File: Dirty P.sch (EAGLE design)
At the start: 23 parts, among them J1 NMJ6HCD2, J2 NMJ6HCD2, SW1 FOOT_SW, U1 MMBT3906, U2 MMBT3906, U3 MMBT3906

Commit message: switched to 4MM caps for 10uF
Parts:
- C1, C6: device MF_Passives:CAPACITOR_P_6.3MM -> MF_Passives:CAPACITOR_P_4MM
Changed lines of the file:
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@@
 <?xml version="1.0" encoding="utf-8"?>
 <!DOCTYPE eagle SYSTEM "eagle.dtd">
-<eagle version="6.6.0">
+<eagle version="6.5.0">
 <drawing>
 <settings>
@@
 <parts>
 <part name="J1" library="PP_Connectors" deviceset="TRS_SWITCHED" device="NMJ6HCD2" value="NMJ6HCD2"/>
-<part name="C1" library="MF_Passives" deviceset="CAPACITOR_P" device="_6.3MM" value="10uF"/>
+<part name="C1" library="MF_Passives" deviceset="CAPACITOR_P" device="_4MM" value="10uF"/>
 <part name="C2" library="MF_Passives" deviceset="CAPACITOR_NP" device="_0805" value="0.1uF"/>
 <part name="R1" library="MF_Passives" deviceset="RESISTOR" device="_0805" value="10K"/>
@@
 <part name="BATT1" library="PP_Connectors" deviceset="BATTERY" device="12BH611-GR" value="12BH611-GR"/>
 <part name="LEVEL" library="PP_Electromechanical" deviceset="POTENTIOMETER" device="PTD901" value="PTD901-2015K-A104"/>
-<part name="C6" library="MF_Passives" deviceset="CAPACITOR_P" device="_6.3MM" value="10uF"/>
+<part name="C6" library="MF_Passives" deviceset="CAPACITOR_P" device="_4MM" value="10uF"/>
 <part name="SW1" library="PP_Electromechanical" deviceset="SPDT" device="FOOT_SW" value="FOOT_SW"/>
 <part name="ATTACK" library="PP_Electromechanical" deviceset="POTENTIOMETER" device="PTD901" value="PTD901-2015K-B102"/>

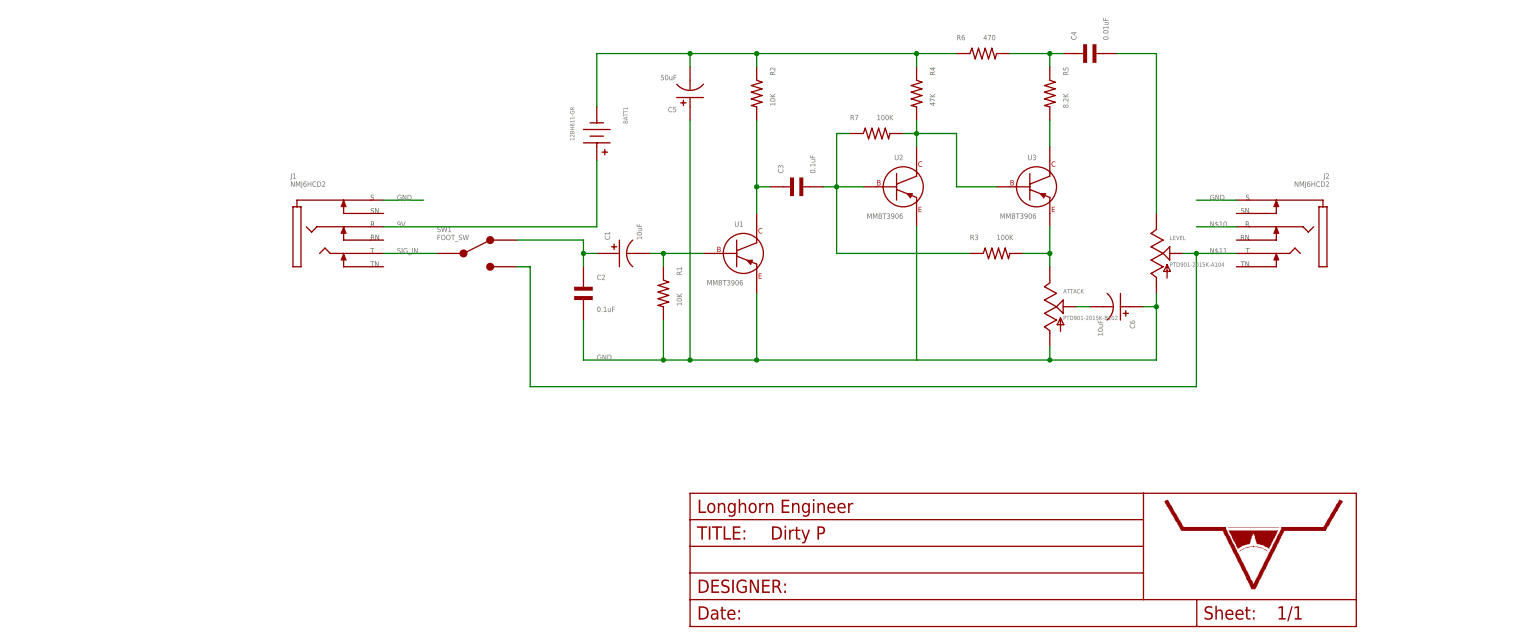
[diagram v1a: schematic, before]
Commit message: REV2: Bass switch. Bias Pot added. Fixed connectors. Added space for Bosses.
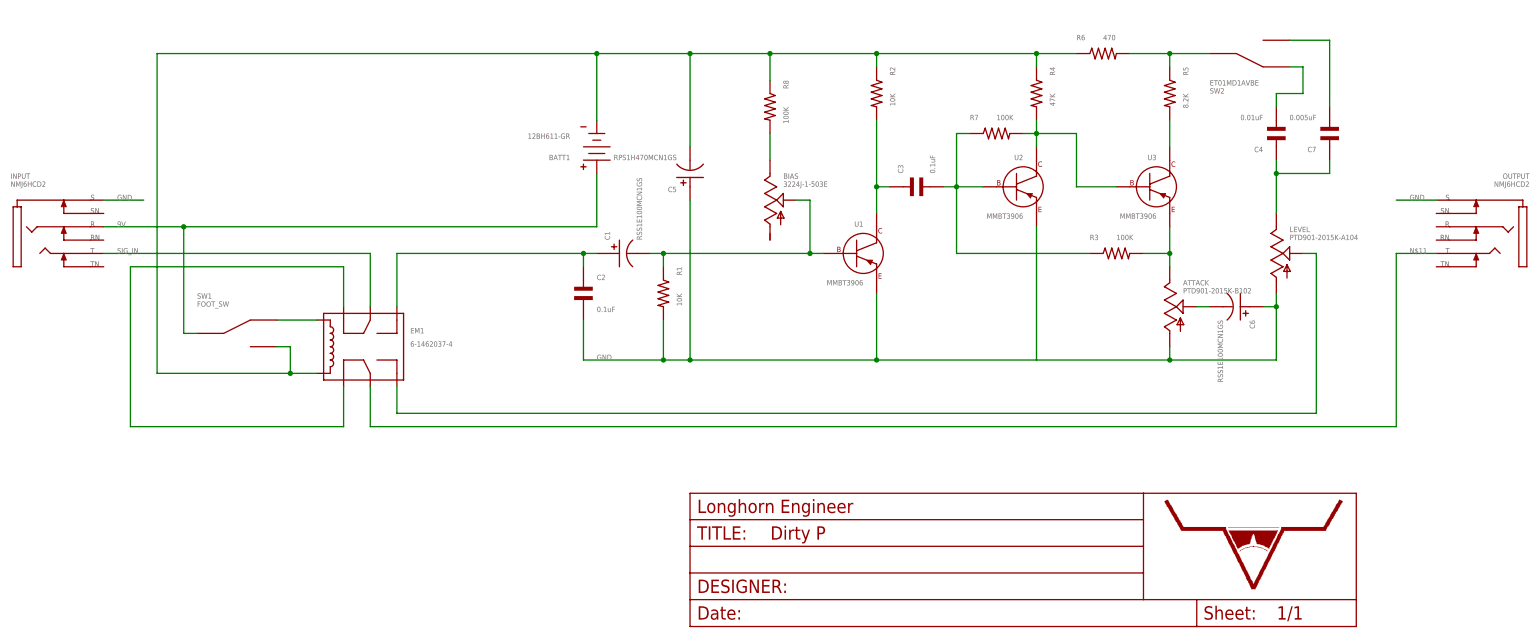
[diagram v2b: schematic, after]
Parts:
- removed J1, J2: NMJ6HCD2, PP_Connectors:TRS_SWITCHEDNMJ6HCD2
- added BIAS: 3224J-1-503E, PP_Passives:POTENTIOMETER_3224J
- added C7: 0.005uF, MF_Passives:CAPACITOR_NP_0805
- added EM1: 6-1462037-4, PP_Electromechanical:DPDT_RELAY_IM_RELAY
- added INPUT, OUTPUT: NMJ6HCD2, PP_Connectors:TRS_SWITCHED_NMJ6HCD2
- added R8: 100K, MF_Passives:RESISTOR_0805
- added SW2: ET01MD1AVBE, PP_Electromechanical:SPDT_ET03MD1AVBE
- BATT1: device PP_Connectors:BATTERY12BH611-GR -> PP_Connectors:BATTERY_12BH611-GR
- C1, C6: value 10uF -> RSS1E100MCN1GS; device MF_Passives:CAPACITOR_P_4MM -> MF_Passives:CAPACITOR_P_6.3MM
- C5: value 50uF -> RPS1H470MCN1GS
- SW1: device PP_Electromechanical:SPDTFOOT_SW -> PP_Electromechanical:SPDT_FOOT_SW
- U$1: REVNUM REV: 1 -> REV: 2
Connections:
- removed net N$10: J2.R
- new net N$12: BIAS.1, R8.P$2
- new net N$15: C4.P$2, SW2.1
- new net N$16: C7.P$2, SW2.2
- new net N$17: EM1.2, EM1.7
- new net N$19: EM1.4, LEVEL.2
- new net N$21: EM1.POS, SW1.1
- net 9V: now also INPUT.R, SW1.C; no longer J1.R
- net GND: now also INPUT.S, OUTPUT.S; no longer J1.S, J2.S
- net N$1: now also BIAS.2
- net N$11: now also EM1.3, OUTPUT.T; no longer J2.T, LEVEL.2, SW1.2
- net N$13: now also C4.P$1, C7.P$1; no longer C4.P$2
- net N$14: now also EM1.5; no longer SW1.1
- net N$4: now also EM1.NEG, R8.P$1, SW1.2
- net N$5: now also SW2.C; no longer C4.P$1
- net SIG_IN: now also EM1.6, INPUT.T; no longer J1.T, SW1.C
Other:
- moved on the sheet: ATTACK, C3, C4, C5, C6, LEVEL, R2, R3, R4, R5, R6, R7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

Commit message: changed out switch and rerouted some stuff.
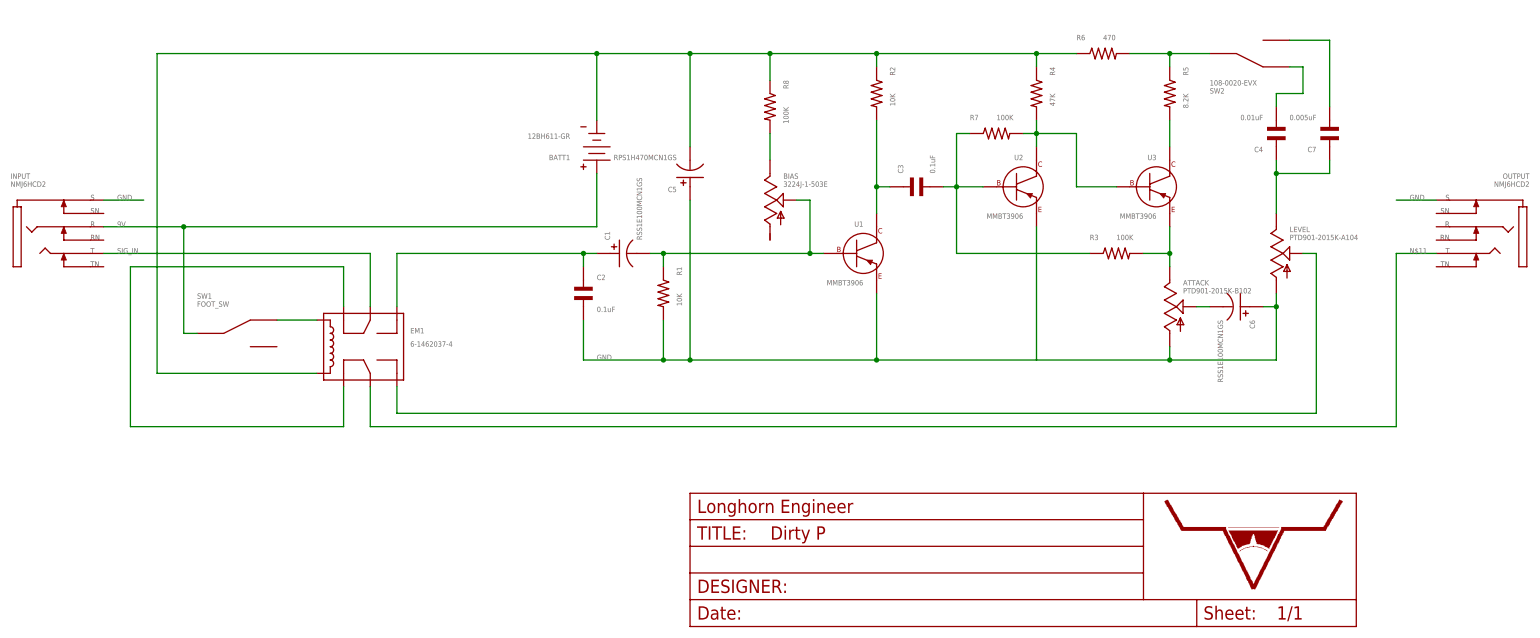
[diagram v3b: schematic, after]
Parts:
- SW2: value ET01MD1AVBE -> 108-0020-EVX; device PP_Electromechanical:SPDT_ET03MD1AVBE -> PP_Electromechanical:SPDT_108-0020-EVX
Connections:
- net N$4: no longer SW1.2
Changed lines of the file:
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@@
 <part name="R8" library="MF_Passives" deviceset="RESISTOR" device="_0805" value="100K"/>
 <part name="BIAS" library="PP_Passives" deviceset="POTENTIOMETER" device="_3224J" value="3224J-1-503E"/>
-<part name="SW2" library="PP_Electromechanical" deviceset="SPDT" device="_ET03MD1AVBE" value="ET01MD1AVBE"/>
+<part name="SW2" library="PP_Electromechanical" deviceset="SPDT" device="_108-0020-EVX" value="108-0020-EVX"/>
 <part name="C7" library="MF_Passives" deviceset="CAPACITOR_NP" device="_0805" value="0.005uF"/>
 <part name="EM1" library="PP_Electromechanical" deviceset="DPDT_RELAY" device="_IM_RELAY" value="6-1462037-4"/>
@@
 <junction x="63.5" y="81.28"/>
 <pinref part="EM1" gate="G$1" pin="NEG"/>
-<wire x1="-22.86" y1="20.32" x2="-27.94" y2="20.32" width="0.1524" layer="91"/>
-<wire x1="-27.94" y1="20.32" x2="-53.34" y2="20.32" width="0.1524" layer="91"/>
+<wire x1="-22.86" y1="20.32" x2="-53.34" y2="20.32" width="0.1524" layer="91"/>
 <wire x1="-53.34" y1="20.32" x2="-53.34" y2="81.28" width="0.1524" layer="91"/>
 <wire x1="-53.34" y1="81.28" x2="30.48" y2="81.28" width="0.1524" layer="91"/>
-<pinref part="SW1" gate="G$1" pin="2"/>
-<wire x1="-30.48" y1="25.4" x2="-27.94" y2="25.4" width="0.1524" layer="91"/>
-<wire x1="-27.94" y1="25.4" x2="-27.94" y2="20.32" width="0.1524" layer="91"/>
-<junction x="-27.94" y="20.32"/>
 <junction x="30.48" y="81.28"/>
 </segment>

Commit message: Changed caps back
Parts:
- added R9: 50K, MF_Passives:RESISTOR_0805
- C1, C6: value RSS1E100MCN1GS -> 10uF; device MF_Passives:CAPACITOR_P_6.3MM -> MF_Passives:CAPACITOR_P_4MM
- C5: value RPS1H470MCN1GS -> 50uF
- C7: value 0.005uF -> 0.001uF
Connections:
- new net N$10: LEVEL.1, R9.P$2
- net N$13: now also R9.P$1; no longer LEVEL.1
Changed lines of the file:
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@@
 <?xml version="1.0" encoding="utf-8"?>
 <!DOCTYPE eagle SYSTEM "eagle.dtd">
-<eagle version="6.6.0">
+<eagle version="6.5.0">
 <drawing>
 <settings>
@@
 <parts>
 <part name="INPUT" library="PP_Connectors" deviceset="TRS_SWITCHED" device="_NMJ6HCD2" value="NMJ6HCD2"/>
-<part name="C1" library="MF_Passives" deviceset="CAPACITOR_P" device="_6.3MM" value="RSS1E100MCN1GS"/>
+<part name="C1" library="MF_Passives" deviceset="CAPACITOR_P" device="_4MM" value="10uF"/>
 <part name="C2" library="MF_Passives" deviceset="CAPACITOR_NP" device="_0805" value="0.1uF"/>
 <part name="R1" library="MF_Passives" deviceset="RESISTOR" device="_0805" value="10K"/>
@@
 <part name="OUTPUT" library="PP_Connectors" deviceset="TRS_SWITCHED" device="_NMJ6HCD2" value="NMJ6HCD2"/>
 <part name="C4" library="MF_Passives" deviceset="CAPACITOR_NP" device="_0805" value="0.01uF"/>
-<part name="C5" library="MF_Passives" deviceset="CAPACITOR_P" device="_8MM" value="RPS1H470MCN1GS"/>
+<part name="C5" library="MF_Passives" deviceset="CAPACITOR_P" device="_8MM" value="50uF"/>
 <part name="R7" library="MF_Passives" deviceset="RESISTOR" device="_0805" value="100K"/>
 <part name="BATT1" library="PP_Connectors" deviceset="BATTERY" device="_12BH611-GR" value="12BH611-GR"/>
 <part name="LEVEL" library="PP_Electromechanical" deviceset="POTENTIOMETER" device="PTD901" value="PTD901-2015K-A104"/>
-<part name="C6" library="MF_Passives" deviceset="CAPACITOR_P" device="_6.3MM" value="RSS1E100MCN1GS"/>
+<part name="C6" library="MF_Passives" deviceset="CAPACITOR_P" device="_4MM" value="10uF"/>
 <part name="SW1" library="PP_Electromechanical" deviceset="SPDT" device="_FOOT_SW" value="FOOT_SW"/>
 <part name="ATTACK" library="PP_Electromechanical" deviceset="POTENTIOMETER" device="PTD901" value="PTD901-2015K-B102"/>
@@
 <part name="BIAS" library="PP_Passives" deviceset="POTENTIOMETER" device="_3224J" value="3224J-1-503E"/>
 <part name="SW2" library="PP_Electromechanical" deviceset="SPDT" device="_108-0020-EVX" value="108-0020-EVX"/>
-<part name="C7" library="MF_Passives" deviceset="CAPACITOR_NP" device="_0805" value="0.005uF"/>
+<part name="C7" library="MF_Passives" deviceset="CAPACITOR_NP" device="_0805" value="0.001uF"/>
 <part name="EM1" library="PP_Electromechanical" deviceset="DPDT_RELAY" device="_IM_RELAY" value="6-1462037-4"/>
+<part name="R9" library="MF_Passives" deviceset="RESISTOR" device="_0805" value="50K"/>
 </parts>
 <sheets>
@@
 <instance part="C7" gate="G$1" x="170.18" y="66.04" rot="R180"/>
 <instance part="EM1" gate="G$1" x="-20.32" y="30.48"/>
+<instance part="R9" gate="G$1" x="152.4" y="53.34"/>
 </instances>
 <busses>
@@
 <net name="N$13" class="0">
 <segment>
-<pinref part="LEVEL" gate="G$1" pin="1"/>
 <wire x1="160.02" y1="60.96" x2="160.02" y2="58.42" width="0.1524" layer="91"/>
 <pinref part="C4" gate="G$1" pin="P$1"/>
 <pinref part="C7" gate="G$1" pin="P$1"/>
-<wire x1="160.02" y1="58.42" x2="160.02" y2="50.8" width="0.1524" layer="91"/>
 <wire x1="160.02" y1="58.42" x2="170.18" y2="58.42" width="0.1524" layer="91"/>
 <wire x1="170.18" y1="58.42" x2="170.18" y2="60.96" width="0.1524" layer="91"/>
+<wire x1="160.02" y1="58.42" x2="144.78" y2="58.42" width="0.1524" layer="91"/>
+<wire x1="144.78" y1="58.42" x2="144.78" y2="53.34" width="0.1524" layer="91"/>
+<pinref part="R9" gate="G$1" pin="P$1"/>
+<wire x1="144.78" y1="53.34" x2="147.32" y2="53.34" width="0.1524" layer="91"/>
 <junction x="160.02" y="58.42"/>
 </segment>
@@
 </segment>
 </net>
+<net name="N$10" class="0">
+<segment>
+<pinref part="R9" gate="G$1" pin="P$2"/>
+<pinref part="LEVEL" gate="G$1" pin="1"/>
+<wire x1="157.48" y1="53.34" x2="160.02" y2="53.34" width="0.1524" layer="91"/>
+<wire x1="160.02" y1="53.34" x2="160.02" y2="50.8" width="0.1524" layer="91"/>
+</segment>
+</net>

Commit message: changed R9 to 51K cause 50K doesnt really exist
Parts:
- R9: value 50K -> 51K
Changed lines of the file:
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@@
 <grid distance="0.1" unitdist="inch" unit="inch" style="lines" multiple="1" display="no" altdistance="0.01" altunitdist="inch" altunit="inch"/>
 <layers>
-<layer number="1" name="Top" color="4" fill="1" visible="yes" active="no"/>
-<layer number="2" name="Route2" color="1" fill="3" visible="yes" active="no"/>
-<layer number="3" name="Route3" color="4" fill="3" visible="yes" active="no"/>
-<layer number="4" name="Route4" color="1" fill="4" visible="yes" active="no"/>
-<layer number="5" name="Route5" color="4" fill="4" visible="yes" active="no"/>
-<layer number="6" name="Route6" color="1" fill="8" visible="yes" active="no"/>
-<layer number="7" name="Route7" color="4" fill="8" visible="yes" active="no"/>
-<layer number="8" name="Route8" color="1" fill="2" visible="yes" active="no"/>
-<layer number="9" name="Route9" color="4" fill="2" visible="yes" active="no"/>
-<layer number="10" name="Route10" color="1" fill="7" visible="yes" active="no"/>
-<layer number="11" name="Route11" color="4" fill="7" visible="yes" active="no"/>
-<layer number="12" name="Route12" color="1" fill="5" visible="yes" active="no"/>
-<layer number="13" name="Route13" color="4" fill="5" visible="yes" active="no"/>
-<layer number="14" name="Route14" color="1" fill="6" visible="yes" active="no"/>
-<layer number="15" name="Route15" color="4" fill="6" visible="yes" active="no"/>
-<layer number="16" name="Bottom" color="1" fill="1" visible="yes" active="no"/>
-<layer number="17" name="Pads" color="2" fill="1" visible="yes" active="no"/>
-<layer number="18" name="Vias" color="2" fill="1" visible="yes" active="no"/>
-<layer number="19" name="Unrouted" color="6" fill="1" visible="yes" active="no"/>
-<layer number="20" name="Dimension" color="15" fill="1" visible="yes" active="no"/>
-<layer number="21" name="tPlace" color="7" fill="1" visible="yes" active="no"/>
-<layer number="22" name="bPlace" color="7" fill="1" visible="yes" active="no"/>
-<layer number="23" name="tOrigins" color="15" fill="1" visible="yes" active="no"/>
-<layer number="24" name="bOrigins" color="15" fill="1" visible="yes" active="no"/>
-<layer number="25" name="tNames" color="7" fill="1" visible="yes" active="no"/>
-<layer number="26" name="bNames" color="7" fill="1" visible="yes" active="no"/>
-<layer number="27" name="tValues" color="7" fill="1" visible="yes" active="no"/>
-<layer number="28" name="bValues" color="7" fill="1" visible="yes" active="no"/>
+<layer number="1" name="Top" color="4" fill="1" visible="no" active="no"/>
+<layer number="2" name="Route2" color="1" fill="3" visible="no" active="no"/>
+<layer number="3" name="Route3" color="4" fill="3" visible="no" active="no"/>
+<layer number="4" name="Route4" color="1" fill="4" visible="no" active="no"/>
+<layer number="5" name="Route5" color="4" fill="4" visible="no" active="no"/>
+<layer number="6" name="Route6" color="1" fill="8" visible="no" active="no"/>
+<layer number="7" name="Route7" color="4" fill="8" visible="no" active="no"/>
+<layer number="8" name="Route8" color="1" fill="2" visible="no" active="no"/>
+<layer number="9" name="Route9" color="4" fill="2" visible="no" active="no"/>
+<layer number="10" name="Route10" color="1" fill="7" visible="no" active="no"/>
+<layer number="11" name="Route11" color="4" fill="7" visible="no" active="no"/>
+<layer number="12" name="Route12" color="1" fill="5" visible="no" active="no"/>
+<layer number="13" name="Route13" color="4" fill="5" visible="no" active="no"/>
+<layer number="14" name="Route14" color="1" fill="6" visible="no" active="no"/>
+<layer number="15" name="Route15" color="4" fill="6" visible="no" active="no"/>
+<layer number="16" name="Bottom" color="1" fill="1" visible="no" active="no"/>
+<layer number="17" name="Pads" color="2" fill="1" visible="no" active="no"/>
+<layer number="18" name="Vias" color="2" fill="1" visible="no" active="no"/>
+<layer number="19" name="Unrouted" color="6" fill="1" visible="no" active="no"/>
+<layer number="20" name="Dimension" color="15" fill="1" visible="no" active="no"/>
+<layer number="21" name="tPlace" color="7" fill="1" visible="no" active="no"/>
+<layer number="22" name="bPlace" color="7" fill="1" visible="no" active="no"/>
+<layer number="23" name="tOrigins" color="15" fill="1" visible="no" active="no"/>
+<layer number="24" name="bOrigins" color="15" fill="1" visible="no" active="no"/>
+<layer number="25" name="tNames" color="7" fill="1" visible="no" active="no"/>
+<layer number="26" name="bNames" color="7" fill="1" visible="no" active="no"/>
+<layer number="27" name="tValues" color="7" fill="1" visible="no" active="no"/>
+<layer number="28" name="bValues" color="7" fill="1" visible="no" active="no"/>
 <layer number="29" name="tStop" color="7" fill="3" visible="no" active="no"/>
 <layer number="30" name="bStop" color="7" fill="6" visible="no" active="no"/>
@@
 <layer number="35" name="tGlue" color="7" fill="4" visible="no" active="no"/>
 <layer number="36" name="bGlue" color="7" fill="5" visible="no" active="no"/>
-<layer number="37" name="tTest" color="7" fill="1" visible="yes" active="no"/>
-<layer number="38" name="bTest" color="7" fill="1" visible="yes" active="no"/>
+<layer number="37" name="tTest" color="7" fill="1" visible="no" active="no"/>
+<layer number="38" name="bTest" color="7" fill="1" visible="no" active="no"/>
 <layer number="39" name="tKeepout" color="4" fill="11" visible="no" active="no"/>
 <layer number="40" name="bKeepout" color="1" fill="11" visible="no" active="no"/>
@@
 <layer number="44" name="Drills" color="7" fill="1" visible="no" active="no"/>
 <layer number="45" name="Holes" color="7" fill="1" visible="no" active="no"/>
-<layer number="46" name="Milling" color="3" fill="1" visible="yes" active="no"/>
-<layer number="47" name="Measures" color="7" fill="1" visible="yes" active="no"/>
-<layer number="48" name="Document" color="7" fill="1" visible="yes" active="no"/>
-<layer number="49" name="Reference" color="7" fill="1" visible="yes" active="no"/>
-<layer number="50" name="dxf" color="7" fill="1" visible="yes" active="no"/>
-<layer number="51" name="tDocu" color="7" fill="1" visible="yes" active="no"/>
-<layer number="52" name="bDocu" color="7" fill="1" visible="yes" active="no"/>
-<layer number="53" name="tGND_GNDA" color="7" fill="9" visible="yes" active="no"/>
-<layer number="54" name="bGND_GNDA" color="1" fill="9" visible="yes" active="no"/>
-<layer number="56" name="wert" color="7" fill="1" visible="yes" active="no"/>
+<layer number="46" name="Milling" color="3" fill="1" visible="no" active="no"/>
+<layer number="47" name="Measures" color="7" fill="1" visible="no" active="no"/>
+<layer number="48" name="Document" color="7" fill="1" visible="no" active="no"/>
+<layer number="49" name="Reference" color="7" fill="1" visible="no" active="no"/>
+<layer number="50" name="dxf" color="7" fill="1" visible="no" active="no"/>
+<layer number="51" name="tDocu" color="7" fill="1" visible="no" active="no"/>
+<layer number="52" name="bDocu" color="7" fill="1" visible="no" active="no"/>
+<layer number="53" name="tGND_GNDA" color="7" fill="9" visible="no" active="no"/>
+<layer number="54" name="bGND_GNDA" color="1" fill="9" visible="no" active="no"/>
+<layer number="56" name="wert" color="7" fill="1" visible="no" active="no"/>
 <layer number="91" name="Nets" color="2" fill="1" visible="yes" active="yes"/>
 <layer number="92" name="Busses" color="1" fill="1" visible="yes" active="yes"/>
@@
 <part name="C7" library="MF_Passives" deviceset="CAPACITOR_NP" device="_0805" value="0.001uF"/>
 <part name="EM1" library="PP_Electromechanical" deviceset="DPDT_RELAY" device="_IM_RELAY" value="6-1462037-4"/>
-<part name="R9" library="MF_Passives" deviceset="RESISTOR" device="_0805" value="50K"/>
+<part name="R9" library="MF_Passives" deviceset="RESISTOR" device="_0805" value="51K"/>
 </parts>
 <sheets>
